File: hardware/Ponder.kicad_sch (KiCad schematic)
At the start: 54 parts, among them J1 USB_C_Receptacle_USB2.0, J2 SM03B-SRSS-TB, J3 Conn_ARM_JTAG_SWD_10, SW1 SW_Push, SW2 SW_Push, U1 NCP1117-3.3_SOT223, U2 W25Q128JVS, U3 RP2350_80QFN, X1 ABM8-272-T3

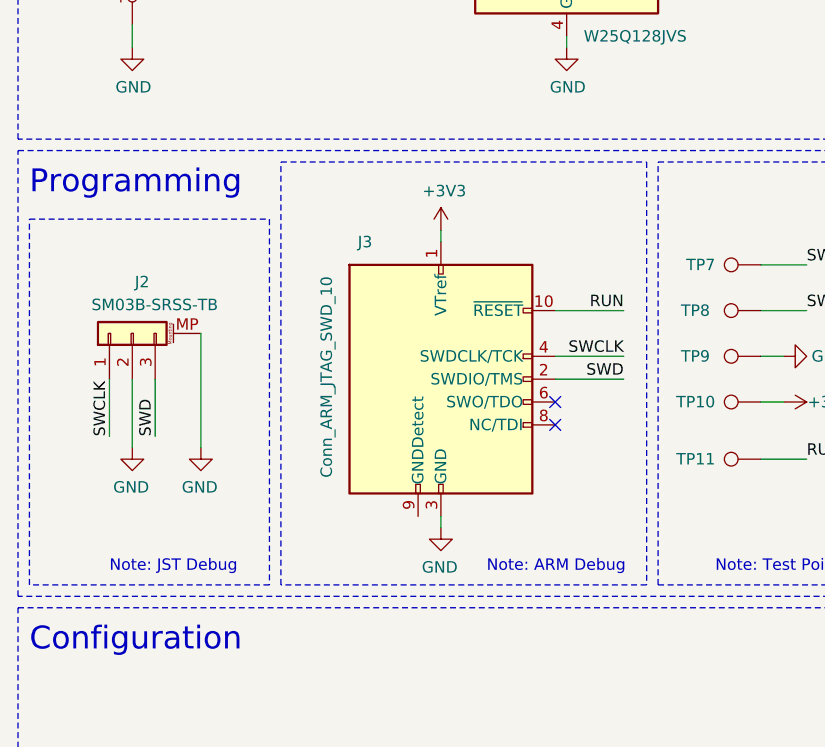
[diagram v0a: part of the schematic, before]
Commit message: Adding modstrike box
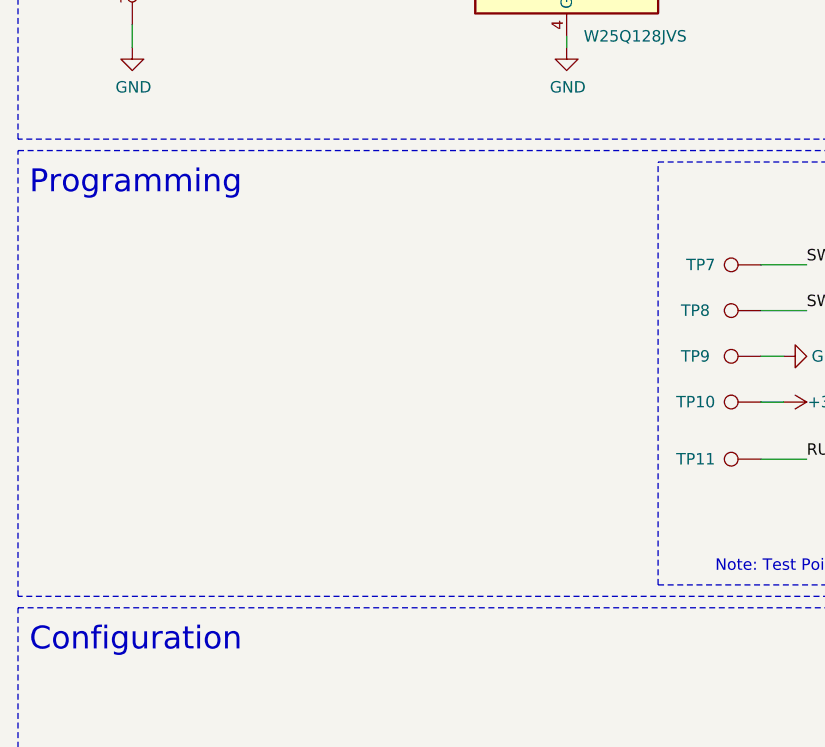
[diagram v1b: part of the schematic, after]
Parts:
- removed J2: SM03B-SRSS-TB, Connector_JST:JST_SH_SM03B-SRSS-TB_1x03-1MP_P1.00mm_Horizontal, symbol Connector_Generic_MountingPin:Conn_01x03_MountingPin
- removed J3: Conn_ARM_JTAG_SWD_10, Connector_PinHeader_1.27mm:PinHeader_2x05_P1.27mm_Vertical_SMD, symbol Connector:Conn_ARM_JTAG_SWD_10
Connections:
- no-connect marks 4 -> 2
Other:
- note removed: "Note: ARM Debug"
- note removed: "Note: JST Debug"

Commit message: Adding ISOs and 4P headers
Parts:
- added C21, C22, C23, C24, C25, C26, C27, C28, C29, C30, C31, C32: 100n, Capacitor_SMD:C_0402_1005Metric, symbol Device:C
- added G1: ModStrike, Ponder:ModStrike, symbol Ponder:GraphicElement
- added G2: Crest, Ponder:Crest-10mm, symbol Ponder:GraphicElement
- added J2, J3, J4, J5, J6, J7: 2.54 HDR, Connector_PinHeader_2.54mm:PinHeader_1x04_P2.54mm_Horizontal, symbol Connector_Generic:Conn_01x04
- added R10, R11, R12, R13, R14, R15, R16, R17, R18, R19, R20, R21: 50, Resistor_SMD:R_0402_1005Metric, symbol Device:R
- added U4, U5, U6, U7, U8, U9: 18012115411H, Package_SO:SOIC-8_3.9x4.9mm_P1.27mm, symbol Isolator:ADuM1201WS
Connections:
- net +3V3: now also C21.1, C23.1, C25.1, C26.1, C29.1, C30.1, U4.1 (VDD1), U5.1 (VDD1), U6.1 (VDD1), U7.1 (VDD1), U8.1 (VDD1), U9.1 (VDD1)
- net GND: now also C21.2, C23.2, C25.2, C26.2, C29.2, C30.2, U4.4 (GND1), U5.4 (GND1), U6.4 (GND1), U7.4 (GND1), U8.4 (GND1), U9.4 (GND1)
- new net: J4.2 (Pin_2), R14.1
- new net: J5.3 (Pin_3), R17.1
- new net: J7.3 (Pin_3), R21.1
- new net: J6.2 (Pin_2), R18.1
- new net: J6.3 (Pin_3), R19.1
- new net: J7.2 (Pin_2), R20.1
- new net: J4.3 (Pin_3), R15.1
- new net: J5.2 (Pin_2), R16.1
- new net: J3.2 (Pin_2), R12.1
- new net: J3.3 (Pin_3), R13.1
- new net: J2.2 (Pin_2), R10.1
- new net: J2.3 (Pin_3), R11.1
- new net DUT0_GND: C22.2, J2.4 (Pin_4), U4.5 (GND2)
- new net DUT0_RX: R11.2, U4.6 (VOB)
- new net DUT0_TX: R10.2, U4.7 (VIA)
- new net DUT0_VCC: C22.1, J2.1 (Pin_1), U4.8 (VDD2)
- new net DUT1_GND: C24.2, J3.4 (Pin_4), U5.5 (GND2)
- new net DUT1_RX: R13.2, U5.6 (VOB)
- new net DUT1_TX: R12.2, U5.7 (VIA)
- new net DUT1_VCC: C24.1, J3.1 (Pin_1), U5.8 (VDD2)
- new net DUT2_GND: C27.2, J4.4 (Pin_4), U6.5 (GND2)
- new net DUT2_RX: R15.2, U6.6 (VOB)
- new net DUT2_TX: R14.2, U6.7 (VIA)
- new net DUT2_VCC: C27.1, J4.1 (Pin_1), U6.8 (VDD2)
- new net DUT3_GND: C28.2, J5.4 (Pin_4), U7.5 (GND2)
- new net DUT3_RX: R17.2, U7.6 (VOB)
- new net DUT3_TX: R16.2, U7.7 (VIA)
- new net DUT3_VCC: C28.1, J5.1 (Pin_1), U7.8 (VDD2)
- new net DUT4_GND: C31.2, J6.4 (Pin_4), U8.5 (GND2)
- new net DUT4_RX: R19.2, U8.6 (VOB)
- new net DUT4_TX: R18.2, U8.7 (VIA)
- new net DUT4_VCC: C31.1, J6.1 (Pin_1), U8.8 (VDD2)
- new net DUT5_GND: C32.2, J7.4 (Pin_4), U9.5 (GND2)
- new net DUT5_RX: R21.2, U9.6 (VOB)
- new net DUT5_TX: R20.2, U9.7 (VIA)
- new net DUT5_VCC: C32.1, J7.1 (Pin_1), U9.8 (VDD2)
- new net ISO_UART0_RX: U4.2 (VOA)
- new net ISO_UART0_TX: U4.3 (VIB)
- new net ISO_UART1_RX: U5.2 (VOA)
- new net ISO_UART1_TX: U5.3 (VIB)
- new net ISO_UART2_RX: U6.2 (VOA)
- new net ISO_UART2_TX: U6.3 (VIB)
- new net ISO_UART3_RX: U7.2 (VOA)
- new net ISO_UART3_TX: U7.3 (VIB)
- new net ISO_UART4_RX: U8.2 (VOA)
- new net ISO_UART4_TX: U8.3 (VIB)
- new net ISO_UART5_RX: U9.2 (VOA)
- new net ISO_UART5_TX: U9.3 (VIB)

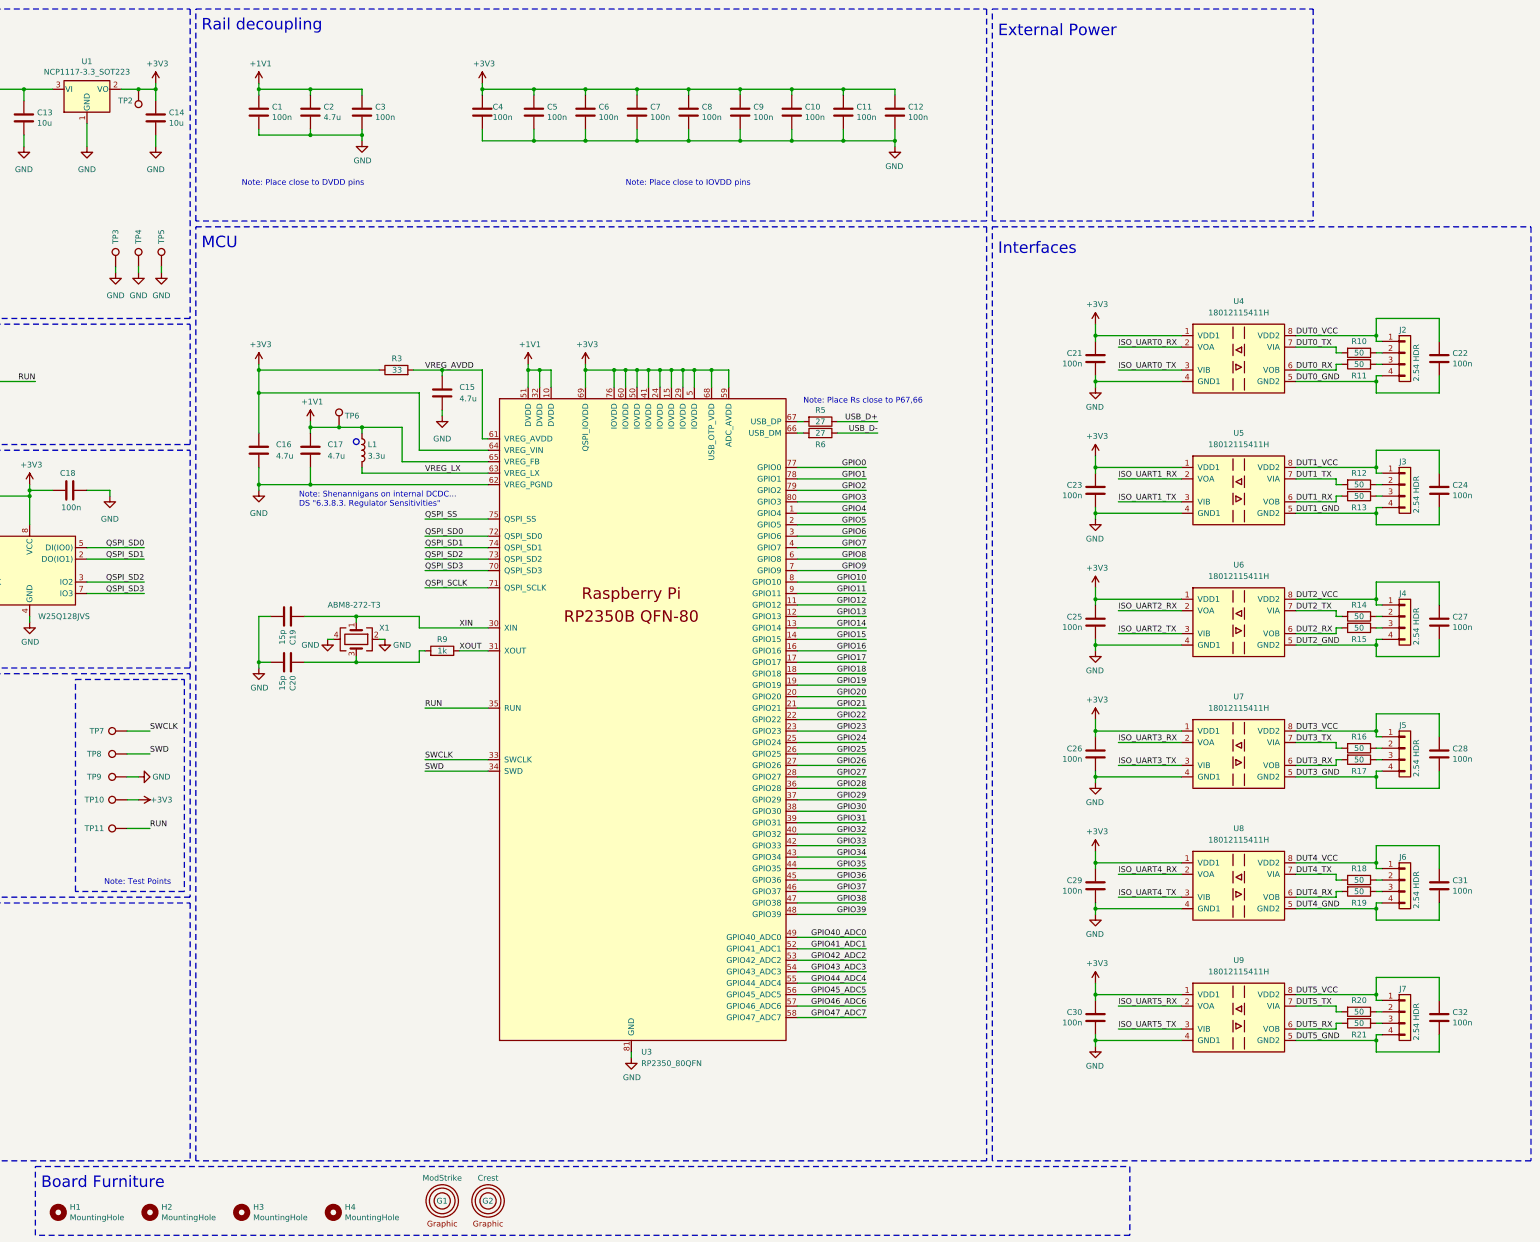
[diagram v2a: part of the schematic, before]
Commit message: Adding pull-ups and LEDs for UARTs. Added nominal I2C and SPI connector along with startes of some selectable off-board low power headers
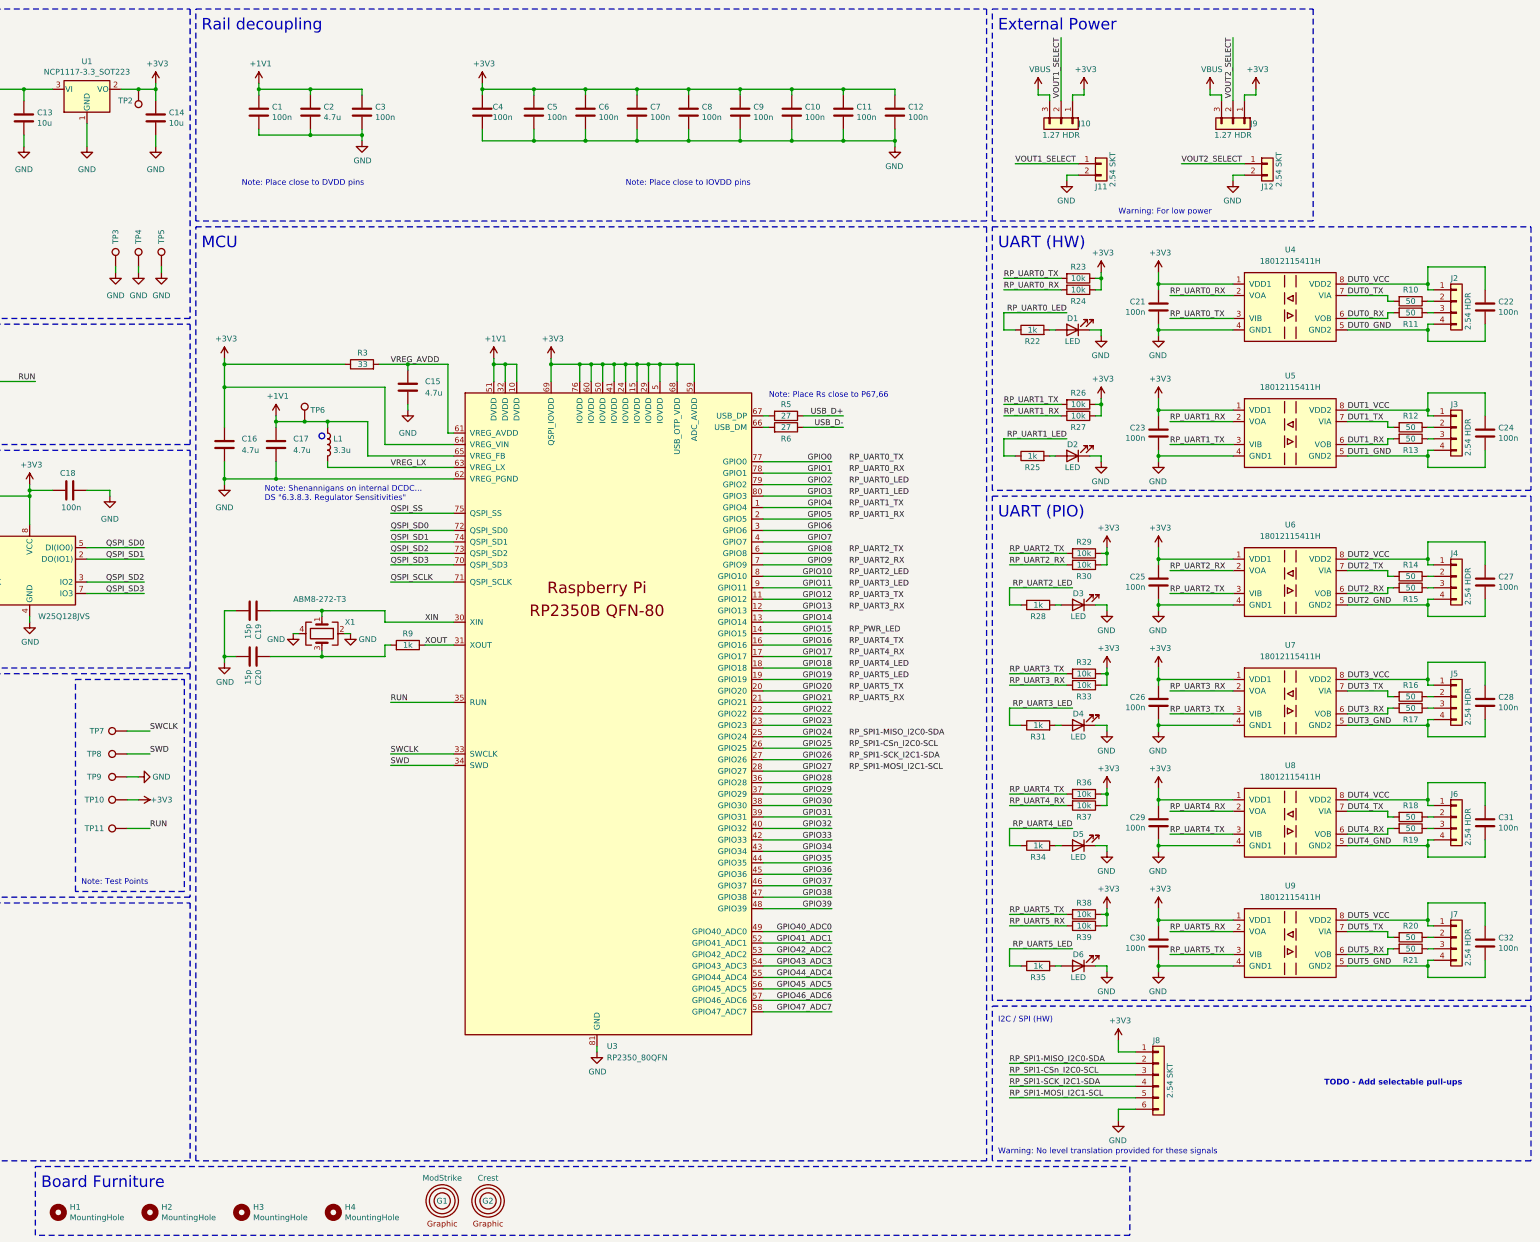
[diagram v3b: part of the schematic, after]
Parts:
- added D1, D2, D3, D4, D5, D6: LED, LED_SMD:LED_0603_1608Metric_Pad1.05x0.95mm_HandSolder, symbol Device:LED
- added J10, J9: 1.27 HDR, Connector_PinHeader_1.27mm:PinHeader_1x03_P1.27mm_Horizontal, symbol Connector_Generic:Conn_01x03
- added J11, J12: 2.54 SKT, Connector_PinSocket_2.54mm:PinSocket_1x02_P2.54mm_Vertical, symbol Connector_Generic:Conn_01x02
- added J8: 2.54 SKT, Connector_PinSocket_2.54mm:PinSocket_1x06_P2.54mm_Horizontal, symbol Connector_Generic:Conn_01x06
- added R22, R25, R28, R31, R34, R35: 1k, Resistor_SMD:R_0402_1005Metric, symbol Device:R
- added R23, R24, R26, R27, R29, R30, R32, R33, R36, R37, R38, R39: 10k, Resistor_SMD:R_0402_1005Metric, symbol Device:R
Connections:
- net +3V3: now also J10.1 (Pin_1), J8.1 (Pin_1), J9.1 (Pin_1), R23.1, R24.1, R26.1, R27.1, R29.1, R30.1, R32.1, R33.1, R36.1, R37.1, R38.1, R39.1
- net GND: now also D1.1 (K), D2.1 (K), D3.1 (K), D4.1 (K), D5.1 (K), D6.1 (K), J11.2 (Pin_2), J12.2 (Pin_2), J8.6 (Pin_6)
- net VBUS: now also J10.3 (Pin_3), J9.3 (Pin_3)
- net ISO_UART0_RX renamed RP_UART0_RX
- net RP_UART0_RX: now also R24.2
- net ISO_UART0_TX renamed RP_UART0_TX
- net RP_UART0_TX: now also R23.2
- net ISO_UART1_RX renamed RP_UART1_RX
- net RP_UART1_RX: now also R27.2
- net ISO_UART1_TX renamed RP_UART1_TX
- net RP_UART1_TX: now also R26.2
- net ISO_UART2_RX renamed RP_UART2_RX
- net RP_UART2_RX: now also R30.2
- net ISO_UART2_TX renamed RP_UART2_TX
- net RP_UART2_TX: now also R29.2
- net ISO_UART3_RX renamed RP_UART3_RX
- net RP_UART3_RX: now also R33.2
- net ISO_UART3_TX renamed RP_UART3_TX
- net RP_UART3_TX: now also R32.2
- net ISO_UART4_RX renamed RP_UART4_RX
- net RP_UART4_RX: now also R37.2
- net ISO_UART4_TX renamed RP_UART4_TX
- net RP_UART4_TX: now also R36.2
- net ISO_UART5_RX renamed RP_UART5_RX
- net RP_UART5_RX: now also R39.2
- net ISO_UART5_TX renamed RP_UART5_TX
- net RP_UART5_TX: now also R38.2
- new net: D6.2 (A), R35.2
- new net: D3.2 (A), R28.2
- new net: D5.2 (A), R34.2
- new net: D2.2 (A), R25.2
- new net: D1.2 (A), R22.2
- new net: D4.2 (A), R31.2
- new net RP_SPI1-CSn_I2C0-SCL: J8.3 (Pin_3)
- new net RP_SPI1-MISO_I2C0-SDA: J8.2 (Pin_2)
- new net RP_SPI1-MOSI_I2C1-SCL: J8.5 (Pin_5)
- new net RP_SPI1-SCK_I2C1-SDA: J8.4 (Pin_4)
- new net RP_UART0_LED: R22.1
- new net RP_UART1_LED: R25.1
- new net RP_UART2_LED: R28.1
- new net RP_UART3_LED: R31.1
- new net RP_UART4_LED: R34.1
- new net RP_UART5_LED: R35.1
- new net VOUT1_SELECT: J10.2 (Pin_2), J11.1 (Pin_1)
- new net VOUT2_SELECT: J12.1 (Pin_1), J9.2 (Pin_2)
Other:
- note added: "I2C / SPI (HW)"
- note added: "TODO - Add selectable pull-ups"
- note added: "UART (HW)"
- note added: "UART (PIO)"
- note added: "Warning: For low power"
- note added: "Warning: No level translation provided for these signals"
- note removed: "Interfaces"
- moved on the sheet: C15, C16, C17, C19, C20, C21, C22, C23, C24, C25, C26, C27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
